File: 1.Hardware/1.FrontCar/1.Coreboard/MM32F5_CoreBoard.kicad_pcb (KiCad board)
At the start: 2 copper layers, 68 parts, among them J1 IPS114, J3 BTB_02x30, J4 BTB_02x30, J5 SH1.0_4P, J7 SH1.0_2P, SW1 3x4, SW2 3x4, SW3 3x4, SW4 3x4, U1 RT9013-33GB, U3 SN65HVD232, U4 SN65HVD232, U5 MM32F5277E9P, U6 MPU-6050, Y1 32.768KHz, Y2 8MHz

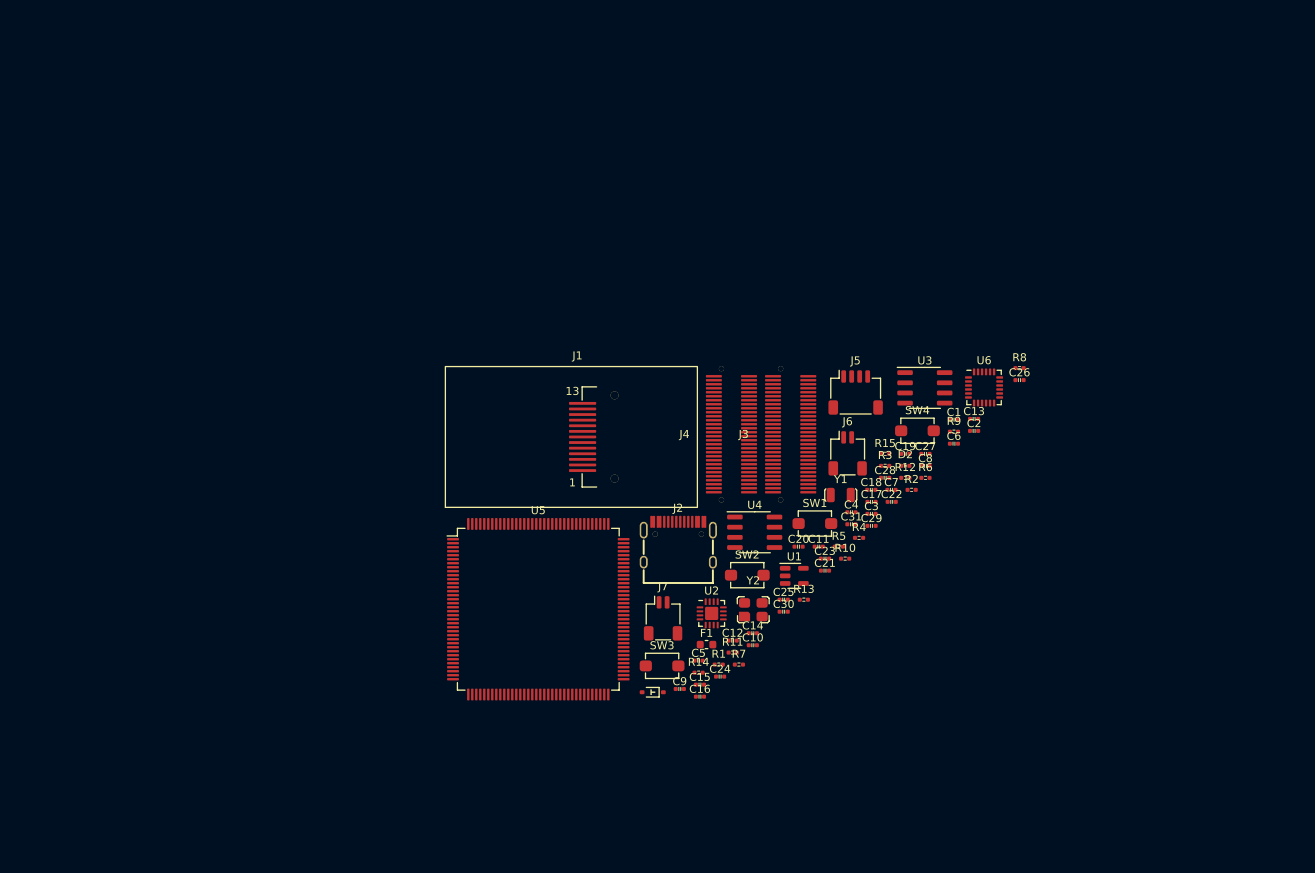
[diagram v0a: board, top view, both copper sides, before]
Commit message: 初步绘制核心板pcb
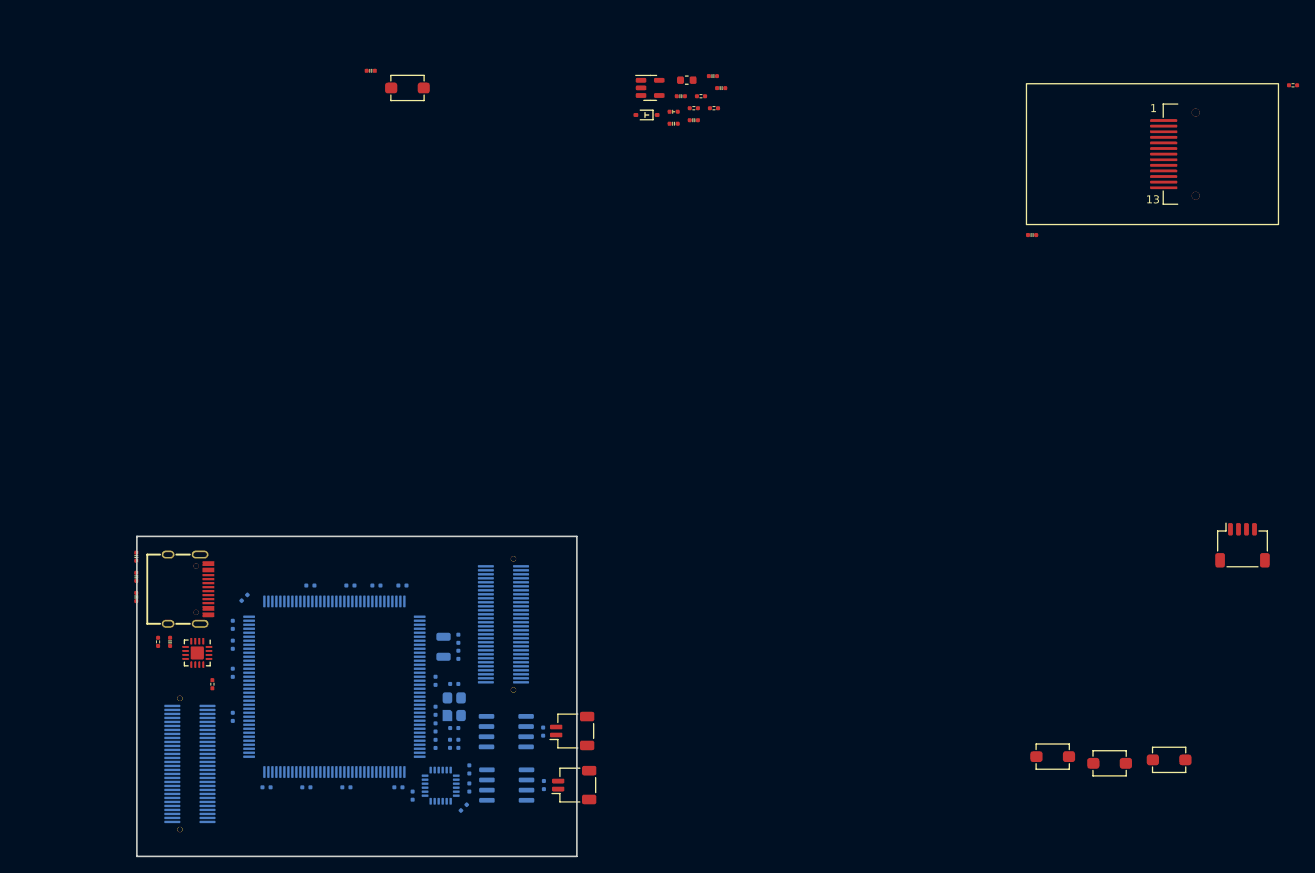
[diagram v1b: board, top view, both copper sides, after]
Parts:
- C11, C12, C13, C14, C15, C16, C17, C18, C19, C20, C21, C22, C23, C25, C26, C27, C28, C29, C30, C31, J3, J4, R10, R11, R12, R13, R14, R15, R7, R8, R9, U3, U4, U5, U6, Y1, Y2: moved to B.Cu
- moved C6 104.0 mm to (63.5, 117.1), turned to -90 degrees
- moved R1 102.0 mm to (208.1, 53.1)
- moved C8 99.6 mm to (63.5, 114.6), turned to -90 degrees
- moved C13 95.3 mm to (84.7, 140.9), turned to 180 degrees
- moved R6 92.8 mm to (73.0, 128.0), turned to -90 degrees
- moved C7 92.2 mm to (67.7, 122.7), turned to -90 degrees
- moved C19 90.1 mm to (79.8, 140.9), turned to 180 degrees
- moved R4 88.6 mm to (66.2, 122.7), turned to -90 degrees
- moved C24 87.4 mm to (92.8, 51.3)
- moved U6 84.2 mm to (101.5, 140.7), turned to -90 degrees
- moved J1 80.8 mm to (191.9, 61.7)
- moved C26 80.2 mm to (103.2, 128.0), turned to 180 degrees
- moved J4 79.2 mm to (70.2, 138.0)
- moved R8 79.1 mm to (114.4, 140.6), turned to 90 degrees
- moved R10 77.0 mm to (75.5, 120.6), turned to 90 degrees
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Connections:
- J7 pad 1: /CAN2_L -> /CAN2_H
- J7 pad 2: /CAN2_H -> /CAN2_L
- J? pad 1: /CAN1_L -> /CAN1_H
- J? pad 2: /CAN1_H -> /CAN1_L
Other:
- board outline added: 55 x 40 mm

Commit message: 布局好累.jpg
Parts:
- added kibuzzard-63A84400: G***, kibuzzard-63A84400, F.Cu at (107.9, 122.4)
- C10, C24, C6, C7, C8, C9, R1, R2, R3, R4, R6, U?: moved to B.Cu
- moved J5 136.1 mm to (68.8, 139.9), turned to -90 degrees
- moved R1 128.1 mm to (103.2, 126.7), turned to 180 degrees
- moved J1 116.7 mm to (92.2, 122.4)
- moved SW2 106.6 mm to (78.6, 139.4)
- moved C1 99.2 mm to (54.4, 116.8)
- moved C2 99.2 mm to (59.4, 115.7)
- moved C4 99.2 mm to (58.4, 114.2)
- moved C5 99.2 mm to (53.5, 120.2)
- moved D1 99.2 mm to (50.1, 119.1)
- moved F1 99.2 mm to (55.1, 114.7)
- moved U1 99.2 mm to (50.5, 115.7)
- moved C3 99.2 mm to (56.0, 119.8)
- moved R5 99.2 mm to (56.0, 118.3)
- moved SW3 94.7 mm to (97.9, 139.5)
- moved D2 93.4 mm to (54.0, 109.9)
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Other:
- board size 55 x 40 mm -> 47.5 x 30.9 mm

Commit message: 完成核心板初步布局
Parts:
- C1, C2, C3, C4, C5, D1, F1, R5, U1: moved to B.Cu
- moved D2 54.6 mm to (108.5, 113.7)
- moved U1 52.8 mm to (103.3, 118.3)
- moved C5 51.1 mm to (104.3, 116.1), turned to 180 degrees
- moved C1 50.1 mm to (104.3, 120.4)
- moved R5 46.3 mm to (102.2, 116.1), turned to 180 degrees
- moved C3 43.4 mm to (99.3, 117.8), turned to 90 degrees
- moved C2 43.1 mm to (102.2, 120.4), turned to 180 degrees
- moved C4 42.3 mm to (100.5, 117.8), turned to 90 degrees
- moved D1 25.8 mm to (75.8, 117.0), turned to 90 degrees
- moved F1 23.2 mm to (78.2, 115.7)
- moved C10 17.2 mm to (87.8, 115.7)
- moved R4 2.61 mm to (74.3, 119.0)
- moved C9 2.33 mm to (74.3, 116.8)
- moved R6 1.98 mm to (74.3, 122.0)
- moved U? 1.61 mm to (69.5, 120.1)
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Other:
- copper layers 2 -> 4

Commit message: 细调
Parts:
- added kibuzzard-63AA82B8: G***, kibuzzard-63AA82B8, F.Cu at (80.6, 65.3)
- added kibuzzard-63AB089E: G***, kibuzzard-63AB089E, F.Cu at (83.7, 71.4)
- added kibuzzard-63AB0AE9: G***, kibuzzard-63AB0AE9, F.Cu at (82.5, 70.9)
- added kibuzzard-63AB0AFB: G***, kibuzzard-63AB0AFB, F.Cu at (82.5, 71.9)
- added kibuzzard-63AB0B00: G***, kibuzzard-63AB0B00, F.Cu at (82.5, 72.9)
- added kibuzzard-63AB0B06: G***, kibuzzard-63AB0B06, F.Cu at (82.5, 69.9)
- added kibuzzard-63AB0F85: G***, kibuzzard-63AB0F85, F.Cu at (116.6, 66.3)
- added kibuzzard-63AB0F9D: G***, kibuzzard-63AB0F9D, F.Cu at (116.6, 72.4)
- added kibuzzard-63AB10B9: G***, kibuzzard-63AB10B9, F.Cu at (121.1, 46.8)
- C30: footprint ErBW_s:C_0402 -> Capacitor_SMD:C_0603_1608Metric
- moved SW1 70.4 mm to (80.6, 61.1)
- moved J4 69.7 mm to (80.2, 65.9)
- moved C1 69.6 mm to (114.5, 51.6)
- moved C2 69.6 mm to (112.4, 51.6)
- moved C3 69.6 mm to (109.5, 49.0)
- moved C4 69.6 mm to (110.7, 49.0)
- moved C5 69.6 mm to (114.5, 47.2)
- moved R5 69.6 mm to (112.4, 47.2)
- moved U1 69.6 mm to (113.5, 49.4)
- moved SW3 69.3 mm to (111.0, 71.4)
- moved R9 69.3 mm to (120.9, 69.4)
- moved U6 69.3 mm to (111.7, 72.2)
- moved C17 69.2 mm to (106.8, 72.5)
- moved SW4 69.2 mm to (100.0, 71.4)
- moved C16 69.2 mm to (85.7, 58.1)
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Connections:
- J3 pad 1: /SWCLK -> GND
- J3 pad 10: /PD1 -> +5VA
- J3 pad 11: /PD3 -> GND
- J3 pad 12: /PG9 -> +5VA
- J3 pad 13: /PG10 -> GND
- J3 pad 14: /PG11 -> +5VA
- J3 pad 15: /PG12 -> GND
- J3 pad 16: /PG13 -> /PE2
- J3 pad 17: /PG14 -> /PE1
- J3 pad 18: /PG15 -> /PE3
- J3 pad 19: /PB3 -> /PE0
- J3 pad 2: /SWDIO -> +5VA
- J3 pad 20: /1LSB -> /PE4
- J3 pad 22: /CAN1_H -> /TOF_SCL
- J3 pad 23: /PE0 -> /1LSB
- J3 pad 24: /CAN1_L -> /TOF_SDA
- J3 pad 25: /PE2 -> /PB3
- J3 pad 26: /PE1 -> /PC13
- J3 pad 27: /PE3 -> /PG15
- J3 pad 28: /PE4 -> /PF0
- J3 pad 29: /TOF_SCL -> /PG14
- J3 pad 3: /UART1_TX -> GND
- J3 pad 30: /TOF_SDA -> /PF1
- J3 pad 31: /PC13 -> /PG13
- J3 pad 32: /PF0 -> /PF2
- J3 pad 33: /PF1 -> /PG12
- J3 pad 34: /PF2 -> /PF3
- J3 pad 35: /PF3 -> /PG11
- J3 pad 37: /PF5 -> /PG10
- J3 pad 38: /PF6 -> /PF5
- J3 pad 39: /PF7 -> /PG9
- J3 pad 4: /UART1_RX -> +5VA
- J3 pad 40: /PF8 -> /PF6
- J3 pad 41: /PF9 -> /PD3
- J3 pad 42: /PF10 -> /PF7
- J3 pad 43: /AUX_SCL -> /PD1
- J3 pad 44: /AUX_SDA -> /PF8
- J3 pad 45: /RST -> /PD0
- J3 pad 46: GND -> /PF9
- J3 pad 47: +5VA -> /PC11
- J3 pad 48: GND -> /PF10
- J3 pad 49: +5VA -> /PC10
- J3 pad 5: /SERVO -> GND
- J3 pad 50: GND -> /ADC_VBAT
- J3 pad 51: +5VA -> /SERVO
- J3 pad 52: GND -> /ADC_DIS
- J3 pad 53: +5VA -> /PH2
- J3 pad 54: GND -> /AUX_SDA
- J3 pad 55: +5VA -> /PB14
- J3 pad 56: GND -> /AUX_SCL
- J3 pad 57: +5VA -> /CAN2_H
- J3 pad 58: GND -> /CAN1_L
- J3 pad 59: +5VA -> /CAN2_L
- J3 pad 6: /PH2 -> +5VA
- J3 pad 60: GND -> /CAN1_H
- J3 pad 7: /PC11 -> GND
- J3 pad 8: /PC10 -> +5VA
- J3 pad 9: /PD0 -> GND
- J4 pad 1: /CAM_TXD -> /PB11
- J4 pad 10: /CAM_D4 -> /CAM_D0
- J4 pad 11: /CAM_D7 -> /MAPLE_CLK
- J4 pad 12: /CAM_D6 -> /CAM_D1
- J4 pad 13: /ELEMAG1 -> /MAPLE_CS
- J4 pad 14: /2PWM -> /CAM_D2
- J4 pad 15: /ELEMAG2 -> /PE10
- J4 pad 16: /2DIR -> /CAM_D3
- J4 pad 17: /ELEMAG3 -> /PE9
- J4 pad 18: /1PWM -> /CAM_D4
- J4 pad 19: /ELEMAG4 -> /PF15
- J4 pad 20: /1DIR -> /CAM_D5
- J4 pad 21: /ELEMAG5 -> /PF14
- J4 pad 22: /ADC_DIS -> /CAM_D6
- J4 pad 23: /PC5 -> /PF13
- J4 pad 24: /ADC_VBAT -> /CAM_D7
- J4 pad 25: /PB1 -> /PF12
- J4 pad 26: /PB0 -> /PB15
- J4 pad 28: /PB2-BOOT1 -> /PD8
- J4 pad 29: /PF13 -> /PB2-BOOT1
- J4 pad 3: /CAM_VSYNC -> /PB10
- J4 pad 30: /PF12 -> /PD9
- J4 pad 31: /PF15 -> /PB1
- J4 pad 32: /PF14 -> /PD10
- J4 pad 33: /PE10 -> /PB0
- J4 pad 34: /PE9 -> /PD11
- J4 pad 35: /MAPLE_CLK -> /PC5
- J4 pad 36: /MAPLE_CS -> /2LSB
- J4 pad 37: /MAPLE_MISO -> /ELEMAG5
- J4 pad 38: /CAN2_L -> /2DIR
- J4 pad 39: /MAPLE_MOSI -> /ELEMAG4
- J4 pad 4: /CAM_RXD -> /CAM_TXD
- J4 pad 40: /CAN2_H -> /PD15
- J4 pad 41: /PB10 -> /ELEMAG3
- J4 pad 42: /PE15 -> /KEY_CENTER
- J4 pad 43: /PB14 -> /ELEMAG2
- J4 pad 44: /PB11 -> /ENCODER_A
- J4 pad 45: /PD8 -> /ELEMAG1
- J4 pad 46: /PB15 -> /ENCODER_B
- J4 pad 47: /PD10 -> /2PWM
- J4 pad 48: /PD9 -> /PC8
- J4 pad 49: /2LSB -> /2DIR
- J4 pad 5: /CAM_D1 -> /PE15
- J4 pad 50: /PD11 -> /PC9
- J4 pad 51: /PD15 -> /1PWM
- J4 pad 52: /2DIR -> /PA8
- J4 pad 53: /ENCODER_A -> /1DIR
- J4 pad 54: /KEY_CENTER -> /PA9
- J4 pad 55: /PC8 -> /UART1_RX
- J4 pad 56: /ENCODER_B -> /PA10
- J4 pad 57: /PA8 -> /UART1_TX
- J4 pad 58: /PC9 -> /SWDIO
- J4 pad 59: /PA10 -> /RST
- J4 pad 6: /CAM_D0 -> /CAM_RXD
- J4 pad 60: /PA9 -> /SWCLK
- J4 pad 7: /CAM_D3 -> /MAPLE_MOSI
- J4 pad 8: /CAM_D2 -> /CAM_VSYNC
- J4 pad 9: /CAM_D5 -> /MAPLE_MISO

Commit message: 信号线布局完成
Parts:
- added G***: LOGO, ErBW_s:ErBW_s_1x1cm, F.Cu at (93.8, 54.7)
- moved R1 15.6 mm to (102.4, 47.2)
- moved C30 2.24 mm to (108.3, 72.2), turned to 90 degrees
- moved R7 0.89 mm to (104.6, 47.2), turned to 180 degrees
- moved C12 0.52 mm to (85.8, 63.1)
- moved C21 0.28 mm to (106.7, 47.2)
- moved C15 0.25 mm to (100.2, 47.2)
- moved C17 0.23 mm to (106.6, 72.5)
- moved C7 0.23 mm to (80.2, 49.3)
- moved U? 0.21 mm to (79.5, 51.9)
- moved U3 0.18 mm to (119.7, 66.3)
- moved U4 0.18 mm to (119.7, 72.4)
- moved C8 0.15 mm to (82.7, 52.1)
- moved U6 0.15 mm to (111.8, 72.2)
- moved C6 0.06 mm to (77.1, 50.9)
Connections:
- net /1LSB renamed /ENC_1LSB
- net /2LSB renamed /ENC_2LSB
- J3 pad 21: /1DIR -> /ENC_1DIR
- J4 pad 38: /2DIR -> /ENC_2DIR
- U5 pad 135: /1DIR -> /ENC_1DIR
- U5 pad 82: /2DIR -> /ENC_2DIR
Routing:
- net /RST: track 0.00 -> 77.8 mm, vias 0 -> 3
- net /PD3: track 0.00 -> 48.9 mm, vias 0 -> 2
- net /PC10: track 0.00 -> 48.7 mm, vias 0 -> 2
- net /PD1: track 0.00 -> 48.5 mm, vias 0 -> 2
- net /SERVO: track 0.00 -> 48.2 mm, vias 0 -> 2
- net /PC11: track 0.00 -> 47.9 mm, vias 0 -> 2
- net /PD0: track 0.00 -> 47.9 mm, vias 0 -> 2
- net /PH2: track 0.00 -> 45.0 mm, vias 0 -> 2
- net +3.3V: track 0.00 -> 44.7 mm
- net /PG9: track 0.00 -> 42.4 mm, vias 0 -> 2
- net /CAN1_D: track 0.00 -> 40.7 mm, vias 0 -> 2
- net +5VA: track 0.00 -> 40.6 mm
- net /PB14: track 0.00 -> 40.5 mm, vias 0 -> 2
- net /ENCODER_B: track 0.00 -> 40.4 mm, vias 0 -> 1
- net /ENCODER_A: track 0.00 -> 39.5 mm, vias 0 -> 1
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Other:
- board text added: "JLCJLCJLCJLC"

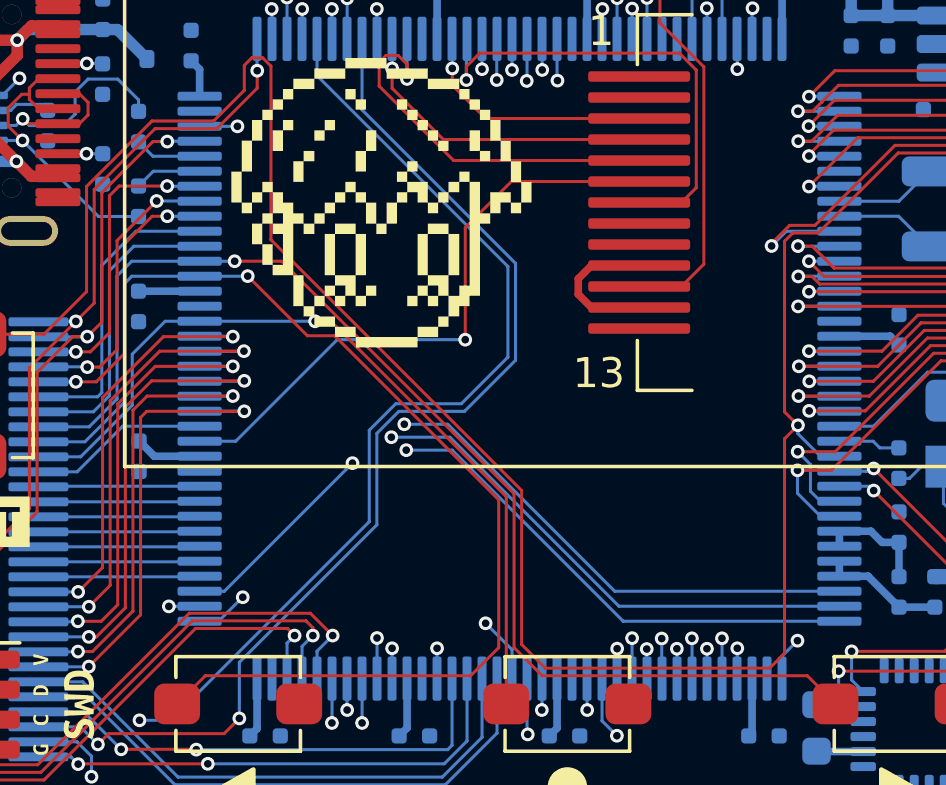
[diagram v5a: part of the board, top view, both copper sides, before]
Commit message: 增加信息丝印
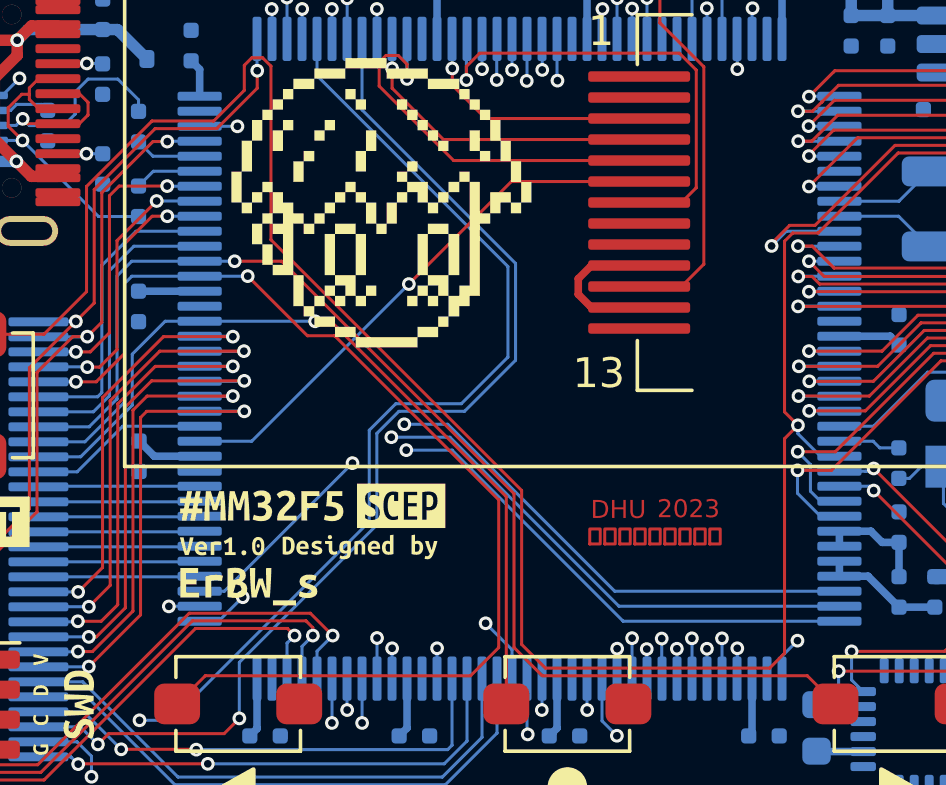
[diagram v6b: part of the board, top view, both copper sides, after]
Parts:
- added kibuzzard-63AD01A8: G***, kibuzzard-63AD01A8, B.Cu at (105.8, 73.9)
- added kibuzzard-63AD0220: G***, kibuzzard-63AD0220, B.Cu at (86.1, 71.6)
- added kibuzzard-63AD04A2: G***, kibuzzard-63AD04A2, F.Cu at (88.5, 66.1)
- added kibuzzard-63AD04A7: G***, kibuzzard-63AD04A7, F.Cu at (93.1, 66.2)
- added kibuzzard-63AD068C: G***, kibuzzard-63AD068C, F.Cu at (94.5, 64.8)
- added kibuzzard-63AD06F8: G***, kibuzzard-63AD06F8, F.Cu at (89.8, 64.8)
- added kibuzzard-63AD073A: G***, kibuzzard-63AD073A, F.Cu at (89.4, 67.5)
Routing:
- net /IPS_RES: track 20.4 -> 18.3 mm
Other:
- board text added: "2023"
- board text added: "DHU"
- board text added: "有人把我队名抢了队"

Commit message: CoreBoard v1.0
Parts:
- removed kibuzzard-63AD068C: G***, kibuzzard-63AD068C
- added kibuzzard-63AD150D: G***, kibuzzard-63AD150D, F.Cu at (94.5, 64.8)
- moved C31 0.38 mm to (115.1, 72.9)
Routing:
- net +3.3V: track 44.7 -> 236.0 mm, vias 0 -> 12
- net /UART1_RX: track 13.8 -> 40.5 mm, vias 2 -> 3
- net /UART1_TX: track 12.6 -> 37.3 mm, vias 2 -> 3
- net /LEDK: track 14.3 -> 17.1 mm
- net /PD15: track 6.00 -> 7.11 mm
- net /PC13: track 11.1 -> 12.1 mm
- net /TOF_SDA: track 10.7 -> 11.7 mm
- net /CAM_D2: track 15.7 -> 16.4 mm
- net /TOF_SCL: track 11.4 -> 12.0 mm
- net GND: vias 0 -> 25
- added copper zone on B.Cu, net GND
- added copper zone on F.Cu, net GND
- added copper zone on In1.Cu, net GND
- added copper zone on In2.Cu, net GND

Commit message: minor changes
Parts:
- removed kibuzzard-63AD04A2: G***, kibuzzard-63AD04A2
- added kibuzzard-63ADB79A: G***, kibuzzard-63ADB79A, F.Cu at (88.5, 66.1)
- moved kibuzzard-63AB10B9 0.20 mm to (120.9, 46.8)
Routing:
- net +3.3V: track 236.0 -> 238.9 mm
